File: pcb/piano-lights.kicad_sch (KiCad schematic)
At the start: 36 parts, among them J1 FTDI RS232, J2 USB_B_Micro, J3 LED Strip, J4 AVR-ISP-6, J5 MIDI IN, J6 MIDI THRU, J7 MIDI Coupler Out, J8 MIDI Coupler In, SW1 Button, SW2 Reset, U1 ATmega328P-P, U2 H11L1, U3 74AHC1G125, Y1 16MHz

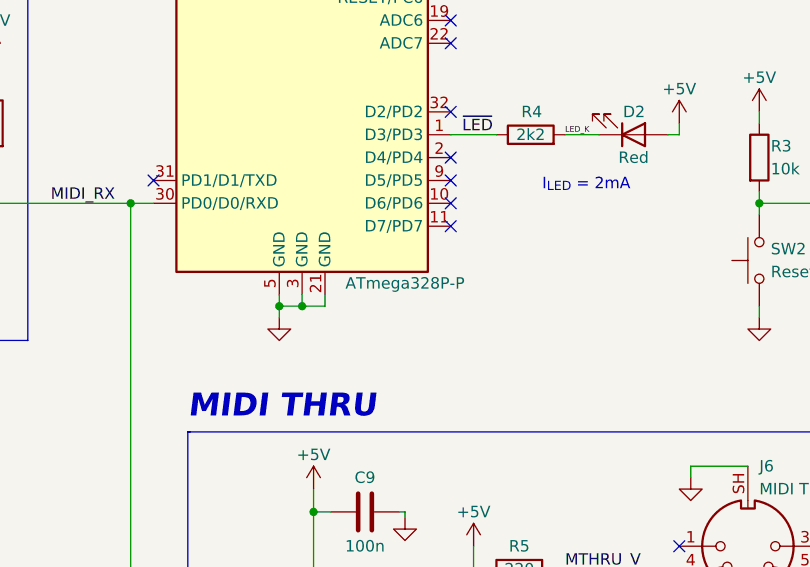
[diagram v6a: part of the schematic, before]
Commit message: Add more Mfr notes
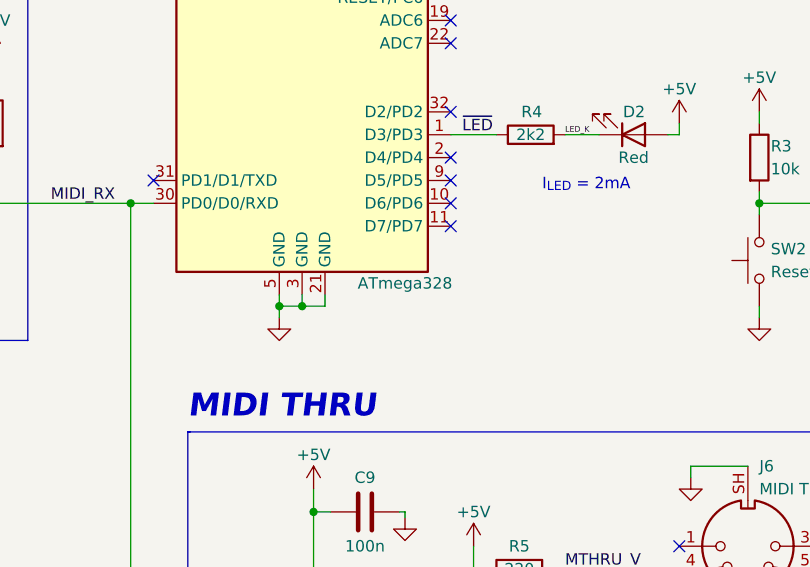
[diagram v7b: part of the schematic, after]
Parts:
- D2: Mfr Part (none) -> 151031SS04000; Part No 151031SS04000 -> (none)
- J2: Mfr Part (none) -> 629105150521; Part No 629105150521 -> (none)
- J4: Mfr (none) -> METZ CONNECT USA Inc.; Mfr Part (none) -> PR20203VBDN; Vendor (none) -> https://www.digikey.com/en/products/detail/metz-connect-usa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
- J5: Mfr (none) -> CUI; Mfr Part (none) -> SDS-50J; Vendor (none) -> https://www.digikey.com/en/products/detail/cui-devices/SDS-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
- J6, J7: Mfr Part (none) -> SDS-50J; Mrf (none) -> CUI; Vendor (none) -> https://www.digikey.com/en/products/detail/cui-devices/SDS-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
- J8: Mfr Part (none) -> SDS-50J; Part No SDS-50J -> (none)
- SW1, SW2: Mfr (none) -> CIT Relay and Switch; Mfr Part (none) -> CT11025.0F160; Vendor (none) -> https://www.digikey.com/en/products/detail/cit-relay-and-sw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
- U1: value ATmega328P-P -> ATmega328; Mfr (none) -> Microchip Technology; Mfr Part (none) -> ATMEGA328-AUR; Vendor (none) -> https://www.digikey.com/en/products/detail/microchip-techno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
- U2: Mfr Part (none) -> H11L1M; Part No. H11L1M -> (none)
- U3: Mfr Part (none) -> 74AHC1G125GV,125; Part No 74AHC1G125GV,125 -> (none)
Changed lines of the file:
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@@
     (in_bom yes) (on_board yes)
     (property "Reference" "U1" (id 0) (at 127 36.83 0))
-    (property "Value" "ATmega328P-P" (id 1) (at 125.73 110.49 0))
+    (property "Value" "ATmega328" (id 1) (at 125.73 110.49 0))
     (property "Footprint" "Package_QFP:TQFP-32_7x7mm_P0.8mm" (id 2) (at 96.52 68.58 0)
       (effects (font (size 1.27 1.27) italic) hide)
     )
     (property "Datasheet" "http://ww1.microchip.com/downloads/en/DeviceDoc/ATmega328_P%20AVR%20MCU%20with%20picoPower%20Technology%20Data%20Sheet%2040001984A.pdf" (id 3) (at 114.3 132.08 0)
+      (effects (font (size 1.27 1.27)) hide)
+    )
+    (property "Mfr" "Microchip Technology" (id 4) (at 114.3 73.66 0)
+      (effects (font (size 1.27 1.27)) hide)
+    )
+    (property "Mfr Part" "ATMEGA328-AUR" (id 5) (at 114.3 73.66 0)
+      (effects (font (size 1.27 1.27)) hide)
+    )
+    (property "Vendor" "https://www.digikey.com/en/products/detail/microchip-technology/ATMEGA328-AUR/2271023" (id 6) (at 114.3 73.66 0)
       (effects (font (size 1.27 1.27)) hide)
     )
@@
       (effects (font (size 1.27 1.27)) hide)
     )
+    (property "Mfr" "CIT Relay and Switch" (id 4) (at 147.32 66.04 0)
+      (effects (font (size 1.27 1.27)) hide)
+    )
+    (property "Mfr Part" "CT11025.0F160" (id 5) (at 147.32 66.04 0)
+      (effects (font (size 1.27 1.27)) hide)
+    )
+    (property "Vendor" "https://www.digikey.com/en/products/detail/cit-relay-and-switch/CT11025-0F160/12418891" (id 6) (at 147.32 66.04 0)
+      (effects (font (size 1.27 1.27)) hide)
+    )
     (pin "1")
     (pin "2")
@@
       (effects (font (size 1.27 1.27)) hide)
     )
-    (property "Mrf" "" (id 4) (at 163.83 139.7 0)
-      (effects (font (size 1.27 1.27)) hide)
-    )
-    (property "Part No" "" (id 5) (at 163.83 139.7 0)
-      (effects (font (size 1.27 1.27)) hide)
-    )
-    (property "Vendor" "" (id 6) (at 163.83 139.7 0)
+    (property "Mrf" "CUI" (id 4) (at 163.83 139.7 0)
+      (effects (font (size 1.27 1.27)) hide)
+    )
+    (property "Mfr Part" "SDS-50J" (id 5) (at 163.83 139.7 0)
+      (effects (font (size 1.27 1.27)) hide)
+    )
+    (property "Vendor" "https://www.digikey.com/en/products/detail/cui-devices/SDS-50J/97033" (id 6) (at 163.83 139.7 0)
       (effects (font (size 1.27 1.27)) hide)
     )
@@
       (effects (font (size 1.27 1.27)) hide)
     )
-    (property "Part No." "H11L1M" (id 5) (at 67.31 101.6 0)
+    (property "Mfr Part" "H11L1M" (id 5) (at 67.31 101.6 0)
       (effects (font (size 1.27 1.27)) hide)
     )
@@
       (effects (font (size 1.27 1.27)) hide)
     )
+    (property "Mfr" "METZ CONNECT USA Inc." (id 4) (at 210.82 99.06 0)
+      (effects (font (size 1.27 1.27)) hide)
+    )
+    (property "Mfr Part" "PR20203VBDN" (id 5) (at 210.82 99.06 0)
+      (effects (font (size 1.27 1.27)) hide)
+    )
+    (property "Vendor" "https://www.digikey.com/en/products/detail/metz-connect-usa-inc/PR20203VBDN/12342894" (id 6) (at 210.82 99.06 0)
+      (effects (font (size 1.27 1.27)) hide)
+    )
     (pin "1")
     (pin "2")
@@
       (effects (font (size 1.27 1.27)) hide)
     )
+    (property "Mfr" "CIT Relay and Switch" (id 4) (at 165.1 107.95 90)
+      (effects (font (size 1.27 1.27)) hide)
+    )
+    (property "Mfr Part" "CT11025.0F160" (id 5) (at 165.1 107.95 90)
+      (effects (font (size 1.27 1.27)) hide)
+    )
+    (property "Vendor" "https://www.digikey.com/en/products/detail/cit-relay-and-switch/CT11025-0F160/12418891" (id 6) (at 165.1 107.95 90)
+      (effects (font (size 1.27 1.27)) hide)
+    )
     (pin "1")
     (pin "2")
@@
     )
     (property "Datasheet" "http://www.mouser.com/ds/2/18/40_c091_abd_e-75918.pdf" (id 3) (at 33.02 104.14 0)
+      (effects (font (size 1.27 1.27)) hide)
+    )
+    (property "Mfr" "CUI" (id 4) (at 33.02 104.14 0)
+      (effects (font (size 1.27 1.27)) hide)
+    )
+    (property "Mfr Part" "SDS-50J" (id 5) (at 33.02 104.14 0)
+      (effects (font (size 1.27 1.27)) hide)
+    )
+    (property "Vendor" "https://www.digikey.com/en/products/detail/cui-devices/SDS-50J/97033" (id 6) (at 33.02 104.14 0)
       (effects (font (size 1.27 1.27)) hide)
     )
@@
       (effects (font (size 1.27 1.27)) hide)
     )
-    (property "Part No" "SDS-50J" (id 5) (at 208.28 145.034 0)
+    (property "Mfr Part" "SDS-50J" (id 5) (at 208.28 145.034 0)
       (effects (font (size 1.27 1.27)) hide)
     )
@@
       (effects (font (size 1.27 1.27)) hide)
     )
-    (property "Part No" "151031SS04000" (id 5) (at 151.13 93.98 0)
+    (property "Mfr Part" "151031SS04000" (id 5) (at 151.13 93.98 0)
       (effects (font (size 1.27 1.27)) hide)
     )
@@
       (effects (font (size 1.27 1.27)) hide)
     )
-    (property "Part No" "74AHC1G125GV,125" (id 5) (at 115.57 149.86 0)
+    (property "Mfr Part" "74AHC1G125GV,125" (id 5) (at 115.57 149.86 0)
       (effects (font (size 1.27 1.27)) hide)
     )
@@
       (effects (font (size 1.27 1.27)) hide)
     )
-    (property "Part No" "629105150521" (id 5) (at 45.72 39.37 0)
+    (property "Mfr Part" "629105150521" (id 5) (at 45.72 39.37 0)
       (effects (font (size 1.27 1.27)) hide)
     )
@@
       (effects (font (size 1.27 1.27)) hide)
     )
-    (property "Mrf" "" (id 4) (at 231.14 144.526 0)
-      (effects (font (size 1.27 1.27)) hide)
-    )
-    (property "Part No" "" (id 5) (at 231.14 144.526 0)
-      (effects (font (size 1.27 1.27)) hide)
-    )
-    (property "Vendor" "" (id 6) (at 231.14 144.526 0)
+    (property "Mrf" "CUI" (id 4) (at 231.14 144.526 0)
+      (effects (font (size 1.27 1.27)) hide)
+    )
+    (property "Mfr Part" "SDS-50J" (id 5) (at 231.14 144.526 0)
+      (effects (font (size 1.27 1.27)) hide)
+    )
+    (property "Vendor" "https://www.digikey.com/en/products/detail/cui-devices/SDS-50J/97033" (id 6) (at 231.14 144.526 0)
       (effects (font (size 1.27 1.27)) hide)
     )
@@
     )
     (path "/3a98d18f-6900-4602-805d-2fb9219ad33a"
-      (reference "U1") (unit 1) (value "ATmega328P-P") (footprint "Package_QFP:TQFP-32_7x7mm_P0.8mm")
+      (reference "U1") (unit 1) (value "ATmega328") (footprint "Package_QFP:TQFP-32_7x7mm_P0.8mm")
     )
     (path "/6eb1a7bf-1572-41ee-b103-299e5107f5f2"

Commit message: Add more Mfr comments. Switch to SMD 0805 LED
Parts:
- D2: footprint LED_THT:LED_D3.0mm -> LED_SMD:LED_0805_2012Metric_Pad1.15x1.40mm_HandSolder; Mfr Würth Elektronik -> Lumex; Mfr Part 151031SS04000 -> SML-LXT0805IW-TR; Vendor https://www.digikey.com/en/products/detail/würth-elektronik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 -> https://www.digikey.com/en/products/detail/lumex-opto-compo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
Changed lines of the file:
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@@
     )
     (property "Value" "Red" (id 1) (at 151.13 96.52 0))
-    (property "Footprint" "LED_THT:LED_D3.0mm" (id 2) (at 151.13 93.98 0)
+    (property "Footprint" "LED_SMD:LED_0805_2012Metric_Pad1.15x1.40mm_HandSolder" (id 2) (at 151.13 93.98 0)
       (effects (font (size 1.27 1.27)) hide)
     )
@@
       (effects (font (size 1.27 1.27)) hide)
     )
-    (property "Mfr" "Würth Elektronik" (id 4) (at 151.13 93.98 0)
-      (effects (font (size 1.27 1.27)) hide)
-    )
-    (property "Mfr Part" "151031SS04000" (id 5) (at 151.13 93.98 0)
-      (effects (font (size 1.27 1.27)) hide)
-    )
-    (property "Vendor" "https://www.digikey.com/en/products/detail/würth-elektronik/151031SS04000/4489979" (id 6) (at 151.13 93.98 0)
+    (property "Mfr" "Lumex" (id 4) (at 151.13 93.98 0)
+      (effects (font (size 1.27 1.27)) hide)
+    )
+    (property "Mfr Part" "SML-LXT0805IW-TR" (id 5) (at 151.13 93.98 0)
+      (effects (font (size 1.27 1.27)) hide)
+    )
+    (property "Vendor" "https://www.digikey.com/en/products/detail/lumex-opto-components-inc/SML-LXT0805IW-TR/304365" (id 6) (at 151.13 93.98 0)
       (effects (font (size 1.27 1.27)) hide)
     )
@@
     )
     (path "/c5692c0b-065d-4eec-ad3f-49f4232dd4aa"
-      (reference "D2") (unit 1) (value "Red") (footprint "LED_THT:LED_D3.0mm")
+      (reference "D2") (unit 1) (value "Red") (footprint "LED_SMD:LED_0805_2012Metric_Pad1.15x1.40mm_HandSolder")
     )
     (path "/5fc6889c-ab79-41f6-aa87-1112c19eb1ab"
